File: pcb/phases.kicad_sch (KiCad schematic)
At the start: 50 parts, among them J13 Conn_01x06_Male, SW18 Reset, SW19 +1, SW20 +10, SW21 -10, SW22 -1, SW23 x2, SW24 /2, SW25 Random, U10 74HC595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

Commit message: layout changes
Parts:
- added J14: Conn_01x04_Male, symbol Connector:Conn_01x04_Male
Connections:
- net Button_serial_out: now also J14.4 (Pin_4)
- net Clock: now also J14.2 (Pin_2)
- net Clock_enable: now also J14.3 (Pin_3)
- net Parallel_Load: now also J14.1 (Pin_1)
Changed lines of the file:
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@@
+    (stroke (width 0) (type default) (color 0 0 0 0))
+  )
+  (wire (pts (xy 78.994 83.312) (xy 99.314 83.312))
     (stroke (width 0) (type default) (color 0 0 0 0))
   )
@@
     (stroke (width 0) (type default) (color 0 0 0 0))
   )
+  (wire (pts (xy 78.994 78.232) (xy 99.314 78.232))
+    (stroke (width 0) (type default) (color 0 0 0 0))
+  )
   (wire (pts (xy 238.252 75.438) (xy 238.252 37.338))
     (stroke (width 0) (type default) (color 0 0 0 0))
@@
     (stroke (width 0) (type default) (color 0 0 0 0))
   )
+  (wire (pts (xy 78.994 80.772) (xy 99.314 80.772))
+    (stroke (width 0) (type default) (color 0 0 0 0))
+  )
   (wire (pts (xy 281.432 105.918) (xy 281.432 108.458))
     (stroke (width 0) (type default) (color 0 0 0 0))
@@
   )
   (wire (pts (xy 28.702 67.818) (xy 28.702 69.088))
+    (stroke (width 0) (type default) (color 0 0 0 0))
+  )
+  (wire (pts (xy 78.994 85.852) (xy 99.314 85.852))
     (stroke (width 0) (type default) (color 0 0 0 0))
   )
@@
     (effects (font (size 1.27 1.27)) (justify left bottom))
   )
+  (hierarchical_label "Clock" (shape input) (at 78.994 80.772 180)
+    (effects (font (size 1.27 1.27)) (justify right))
+  )
+  (hierarchical_label "Button_serial_out" (shape output) (at 78.994 85.852 180)
+    (effects (font (size 1.27 1.27)) (justify right))
+  )
   (hierarchical_label "Storage_Register_Clock" (shape input) (at 172.212 78.486 180)
     (effects (font (size 1.27 1.27)) (justify right))
   )
+  (hierarchical_label "Clock_enable" (shape input) (at 78.994 83.312 180)
+    (effects (font (size 1.27 1.27)) (justify right))
+  )
   (hierarchical_label "Serial_Data_Input" (shape input) (at 172.212 73.406 180)
     (effects (font (size 1.27 1.27)) (justify right))
@@
   )
   (hierarchical_label "Storage_Register_Clock" (shape input) (at 184.912 37.338 180)
+    (effects (font (size 1.27 1.27)) (justify right))
+  )
+  (hierarchical_label "Parallel_Load" (shape input) (at 78.994 78.232 180)
     (effects (font (size 1.27 1.27)) (justify right))
   )
@@
     (pin "1")
   )
+  (symbol (lib_id "Connector:Conn_01x04_Male") (at 104.394 80.772 0) (mirror y) (unit 1)
+    (in_bom yes) (on_board yes) (fields_autoplaced)
+    (property "Reference" "J14" (id 0) (at 105.1052 81.2073 0)
+      (effects (font (size 1.27 1.27)) (justify right))
+    )
+    (property "Value" "Conn_01x04_Male" (id 1) (at 105.1052 83.7442 0)
+      (effects (font (size 1.27 1.27)) (justify right))
+    )
+    (property "Footprint" "" (id 2) (at 104.394 80.772 0)
+      (effects (font (size 1.27 1.27)) hide)
+    )
+    (property "Datasheet" "~" (id 3) (at 104.394 80.772 0)
+      (effects (font (size 1.27 1.27)) hide)
+    )
+    (pin "1")
+    (pin "2")
+    (pin "3")
+    (pin "4")
+  )
   (symbol (lib_id "Device:C") (at 28.702 64.008 0) (unit 1)

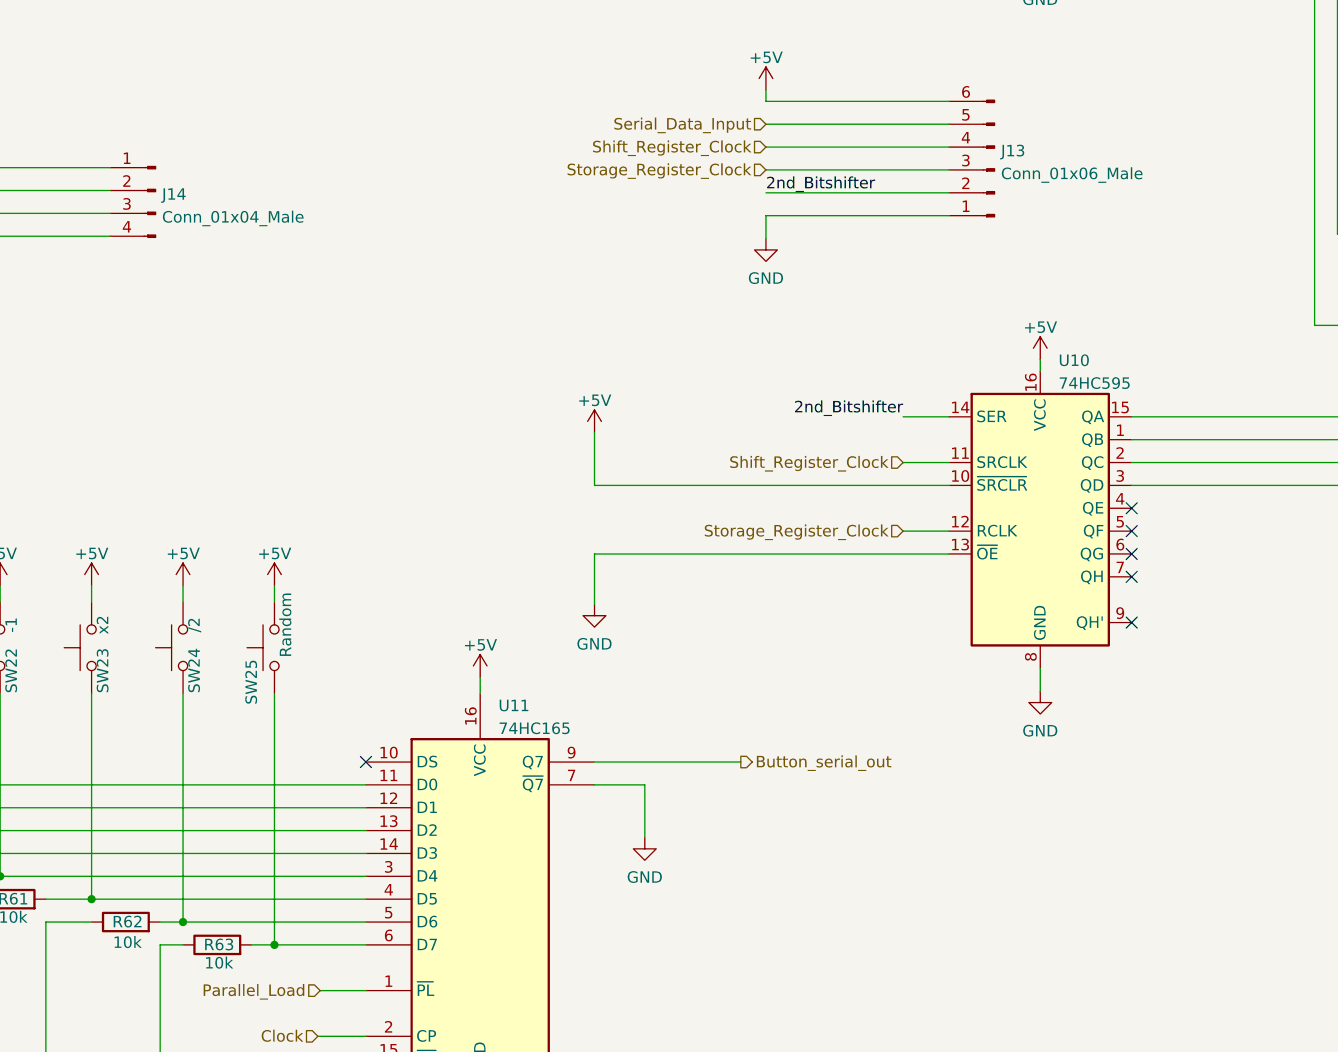
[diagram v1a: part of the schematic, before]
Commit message: moved crystal
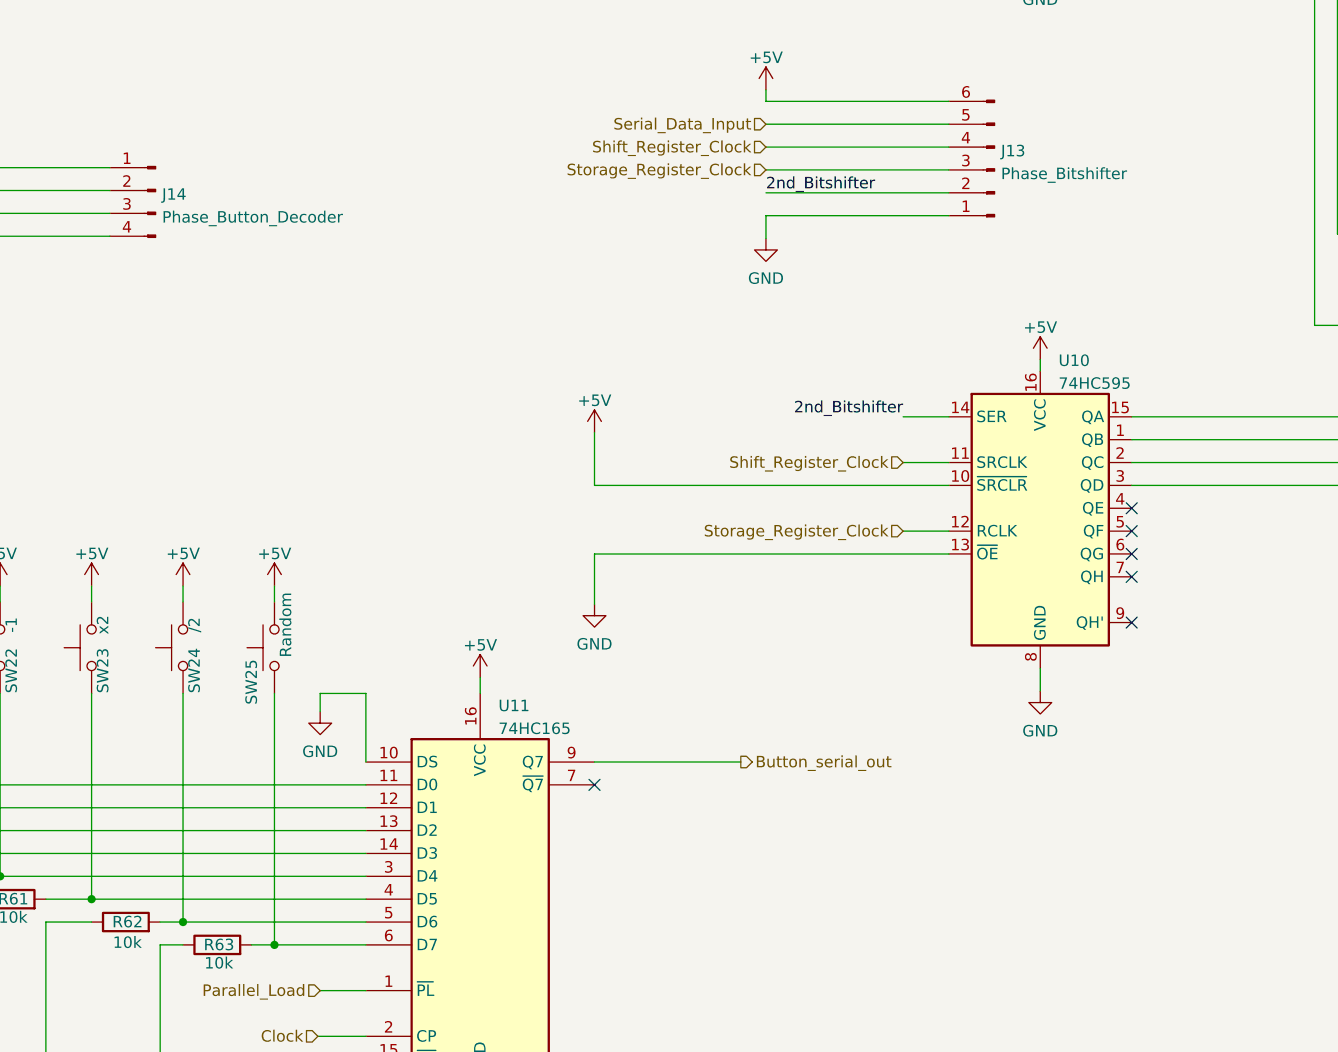
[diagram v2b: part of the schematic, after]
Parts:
- J13: value Conn_01x06_Male -> Phase_Bitshifter
- J14: value Conn_01x04_Male -> Phase_Button_Decoder; footprint (none) -> Connector_PinHeader_2.54mm:PinHeader_1x04_P2.54mm_Vertical
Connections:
- net GND: now also U11.10 (DS); no longer U11.7 (~{Q7})
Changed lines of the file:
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@@
   (no_connect (at 212.852 123.698))
   (no_connect (at 212.852 128.778))
-  (no_connect (at 127.762 144.272))
+  (no_connect (at 153.162 146.812))
   (wire (pts (xy 115.062 164.592) (xy 117.602 164.592))
     (stroke (width 0) (type default) (color 0 0 0 0))
@@
     (stroke (width 0) (type default) (color 0 0 0 0))
   )
+  (wire (pts (xy 122.682 136.652) (xy 122.682 138.684))
+    (stroke (width 0) (type default) (color 0 0 0 0))
+  )
   (wire (pts (xy 46.482 136.652) (xy 46.482 146.812))
     (stroke (width 0) (type default) (color 0 0 0 0))
@@
     (stroke (width 0) (type default) (color 0 0 0 0))
   )
+  (wire (pts (xy 127.762 136.652) (xy 127.762 144.272))
+    (stroke (width 0) (type default) (color 0 0 0 0))
+  )
   (wire (pts (xy 233.172 95.758) (xy 250.952 95.758))
     (stroke (width 0) (type default) (color 0 0 0 0))
@@
     (stroke (width 0) (type default) (color 0 0 0 0))
   )
-  (wire (pts (xy 158.75 146.812) (xy 158.75 152.654))
-    (stroke (width 0) (type default) (color 0 0 0 0))
-  )
   (wire (pts (xy 212.852 47.498) (xy 217.932 47.498))
     (stroke (width 0) (type default) (color 0 0 0 0))
@@
     (stroke (width 0) (type default) (color 0 0 0 0))
   )
+  (wire (pts (xy 122.682 136.652) (xy 127.762 136.652))
+    (stroke (width 0) (type default) (color 0 0 0 0))
+  )
   (wire (pts (xy 212.852 113.538) (xy 245.872 113.538))
     (stroke (width 0) (type default) (color 0 0 0 0))
@@
   )
   (wire (pts (xy 281.432 65.278) (xy 281.432 67.818))
-    (stroke (width 0) (type default) (color 0 0 0 0))
-  )
-  (wire (pts (xy 153.162 146.812) (xy 158.75 146.812))
     (stroke (width 0) (type default) (color 0 0 0 0))
   )
@@
     (pin "1")
   )
+  (symbol (lib_id "power:GND") (at 122.682 138.684 0) (unit 1)
+    (in_bom yes) (on_board yes) (fields_autoplaced)
+    (property "Reference" "#PWR0167" (id 0) (at 122.682 145.034 0)
+      (effects (font (size 1.27 1.27)) hide)
+    )
+    (property "Value" "GND" (id 1) (at 122.682 143.1274 0))
+    (property "Footprint" "" (id 2) (at 122.682 138.684 0)
+      (effects (font (size 1.27 1.27)) hide)
+    )
+    (property "Datasheet" "" (id 3) (at 122.682 138.684 0)
+      (effects (font (size 1.27 1.27)) hide)
+    )
+    (pin "1")
+  )
   (symbol (lib_id "Device:R") (at 270.002 85.598 90) (unit 1)
     (in_bom yes) (on_board yes) (fields_autoplaced)
@@
       (effects (font (size 1.27 1.27)) (justify right))
     )
-    (property "Value" "Conn_01x06_Male" (id 1) (at 198.3232 78.9182 0)
+    (property "Value" "Phase_Bitshifter" (id 1) (at 198.3232 78.9182 0)
       (effects (font (size 1.27 1.27)) (justify right))
     )
@@
     (pin "2")
   )
-  (symbol (lib_id "power:GND") (at 158.75 152.654 0) (unit 1)
-    (in_bom yes) (on_board yes) (fields_autoplaced)
-    (property "Reference" "#PWR081" (id 0) (at 158.75 159.004 0)
-      (effects (font (size 1.27 1.27)) hide)
-    )
-    (property "Value" "GND" (id 1) (at 158.75 157.0974 0))
-    (property "Footprint" "" (id 2) (at 158.75 152.654 0)
-      (effects (font (size 1.27 1.27)) hide)
-    )
-    (property "Datasheet" "" (id 3) (at 158.75 152.654 0)
-      (effects (font (size 1.27 1.27)) hide)
-    )
-    (pin "1")
-  )
   (symbol (lib_id "power:GND") (at 281.432 37.338 0) (unit 1)
     (in_bom yes) (on_board yes) (fields_autoplaced)
@@
       (effects (font (size 1.27 1.27)) (justify right))
     )
-    (property "Value" "Conn_01x04_Male" (id 1) (at 105.1052 83.7442 0)
+    (property "Value" "Phase_Button_Decoder" (id 1) (at 105.1052 83.7442 0)
       (effects (font (size 1.27 1.27)) (justify right))
     )
-    (property "Footprint" "" (id 2) (at 104.394 80.772 0)
-      (effects (font (size 1.27 1.27)) hide)
-    )
+    (property "Footprint" "Connector_PinHeader_2.54mm:PinHeader_1x04_P2.54mm_Vertical" (id 2) (at 104.394 80.772 0)
+      (effects (font (size 1.27 1.27)) hide)
+    )

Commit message: new layout with usb
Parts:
- R44, R45, R46, R47, R48, R49, R50, R51, R52, R53, R54, R55, R56, R57, R58, R59, R60, R61, R62, R63: footprint Resistor_THT:R_Axial_DIN0207_L6.3mm_D2.5mm_P7.62mm_Horizontal -> Resistor_THT:R_Axial_DIN0207_L6.3mm_D2.5mm_P10.16mm_Horizontal
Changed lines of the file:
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@@
     (property "Reference" "R54" (id 0) (at 270.002 121.5222 90))
     (property "Value" "90R" (id 1) (at 270.002 124.0591 90))
-    (property "Footprint" "Resistor_THT:R_Axial_DIN0207_L6.3mm_D2.5mm_P7.62mm_Horizontal" (id 2) (at 270.002 128.016 90)
+    (property "Footprint" "Resistor_THT:R_Axial_DIN0207_L6.3mm_D2.5mm_P10.16mm_Horizontal" (id 2) (at 270.002 128.016 90)
       (effects (font (size 1.27 1.27)) hide)
     )
@@
     (property "Reference" "R44" (id 0) (at 270.002 19.9222 90))
     (property "Value" "90R" (id 1) (at 270.002 22.4591 90))
-    (property "Footprint" "Resistor_THT:R_Axial_DIN0207_L6.3mm_D2.5mm_P7.62mm_Horizontal" (id 2) (at 270.002 26.416 90)
+    (property "Footprint" "Resistor_THT:R_Axial_DIN0207_L6.3mm_D2.5mm_P10.16mm_Horizontal" (id 2) (at 270.002 26.416 90)
       (effects (font (size 1.27 1.27)) hide)
     )
@@
       (effects (font (size 1.27 1.27)) (justify left))
     )
-    (property "Footprint" "Resistor_THT:R_Axial_DIN0207_L6.3mm_D2.5mm_P7.62mm_Horizontal" (id 2) (at 63.246 156.21 90)
+    (property "Footprint" "Resistor_THT:R_Axial_DIN0207_L6.3mm_D2.5mm_P10.16mm_Horizontal" (id 2) (at 63.246 156.21 90)
       (effects (font (size 1.27 1.27)) hide)
     )
@@
       (effects (font (size 1.27 1.27)) (justify left))
     )
-    (property "Footprint" "Resistor_THT:R_Axial_DIN0207_L6.3mm_D2.5mm_P7.62mm_Horizontal" (id 2) (at 101.092 163.83 90)
+    (property "Footprint" "Resistor_THT:R_Axial_DIN0207_L6.3mm_D2.5mm_P10.16mm_Horizontal" (id 2) (at 101.092 163.83 90)
       (effects (font (size 1.27 1.27)) hide)
     )
@@
     (property "Reference" "R50" (id 0) (at 270.002 80.8822 90))
     (property "Value" "90R" (id 1) (at 270.002 83.4191 90))
-    (property "Footprint" "Resistor_THT:R_Axial_DIN0207_L6.3mm_D2.5mm_P7.62mm_Horizontal" (id 2) (at 270.002 87.376 90)
+    (property "Footprint" "Resistor_THT:R_Axial_DIN0207_L6.3mm_D2.5mm_P10.16mm_Horizontal" (id 2) (at 270.002 87.376 90)
       (effects (font (size 1.27 1.27)) hide)
     )
@@
       (effects (font (size 1.27 1.27)) (justify left))
     )
-    (property "Footprint" "Resistor_THT:R_Axial_DIN0207_L6.3mm_D2.5mm_P7.62mm_Horizontal" (id 2) (at 37.592 151.13 90)
+    (property "Footprint" "Resistor_THT:R_Axial_DIN0207_L6.3mm_D2.5mm_P10.16mm_Horizontal" (id 2) (at 37.592 151.13 90)
       (effects (font (size 1.27 1.27)) hide)
     )
@@
     (property "Reference" "R51" (id 0) (at 270.002 91.0422 90))
     (property "Value" "90R" (id 1) (at 270.002 93.5791 90))
-    (property "Footprint" "Resistor_THT:R_Axial_DIN0207_L6.3mm_D2.5mm_P7.62mm_Horizontal" (id 2) (at 270.002 97.536 90)
+    (property "Footprint" "Resistor_THT:R_Axial_DIN0207_L6.3mm_D2.5mm_P10.16mm_Horizontal" (id 2) (at 270.002 97.536 90)
       (effects (font (size 1.27 1.27)) hide)
     )
@@
       (effects (font (size 1.27 1.27)) (justify left))
     )
-    (property "Footprint" "Resistor_THT:R_Axial_DIN0207_L6.3mm_D2.5mm_P7.62mm_Horizontal" (id 2) (at 111.252 166.37 90)
+    (property "Footprint" "Resistor_THT:R_Axial_DIN0207_L6.3mm_D2.5mm_P10.16mm_Horizontal" (id 2) (at 111.252 166.37 90)
       (effects (font (size 1.27 1.27)) hide)
     )
@@
       (effects (font (size 1.27 1.27)) (justify left))
     )
-    (property "Footprint" "Resistor_THT:R_Axial_DIN0207_L6.3mm_D2.5mm_P7.62mm_Horizontal" (id 2) (at 75.692 158.75 90)
+    (property "Footprint" "Resistor_THT:R_Axial_DIN0207_L6.3mm_D2.5mm_P10.16mm_Horizontal" (id 2) (at 75.692 158.75 90)
       (effects (font (size 1.27 1.27)) hide)
     )
@@
     (property "Reference" "R52" (id 0) (at 270.002 101.2022 90))
     (property "Value" "90R" (id 1) (at 270.002 103.7391 90))
-    (property "Footprint" "Resistor_THT:R_Axial_DIN0207_L6.3mm_D2.5mm_P7.62mm_Horizontal" (id 2) (at 270.002 107.696 90)
+    (property "Footprint" "Resistor_THT:R_Axial_DIN0207_L6.3mm_D2.5mm_P10.16mm_Horizontal" (id 2) (at 270.002 107.696 90)
       (effects (font (size 1.27 1.27)) hide)
     )
@@
     (property "Reference" "R46" (id 0) (at 270.002 40.2422 90))
     (property "Value" "90R" (id 1) (at 270.002 42.7791 90))
-    (property "Footprint" "Resistor_THT:R_Axial_DIN0207_L6.3mm_D2.5mm_P7.62mm_Horizontal" (id 2) (at 270.002 46.736 90)
+    (property "Footprint" "Resistor_THT:R_Axial_DIN0207_L6.3mm_D2.5mm_P10.16mm_Horizontal" (id 2) (at 270.002 46.736 90)
       (effects (font (size 1.27 1.27)) hide)
     )
@@
     (property "Reference" "R49" (id 0) (at 270.002 70.7222 90))
     (property "Value" "90R" (id 1) (at 270.002 73.2591 90))
-    (property "Footprint" "Resistor_THT:R_Axial_DIN0207_L6.3mm_D2.5mm_P7.62mm_Horizontal" (id 2) (at 270.002 77.216 90)
+    (property "Footprint" "Resistor_THT:R_Axial_DIN0207_L6.3mm_D2.5mm_P10.16mm_Horizontal" (id 2) (at 270.002 77.216 90)
       (effects (font (size 1.27 1.27)) hide)
     )
@@
     (property "Reference" "R48" (id 0) (at 270.002 60.5622 90))
     (property "Value" "90R" (id 1) (at 270.002 63.0991 90))
-    (property "Footprint" "Resistor_THT:R_Axial_DIN0207_L6.3mm_D2.5mm_P7.62mm_Horizontal" (id 2) (at 270.002 67.056 90)
+    (property "Footprint" "Resistor_THT:R_Axial_DIN0207_L6.3mm_D2.5mm_P10.16mm_Horizontal" (id 2) (at 270.002 67.056 90)
       (effects (font (size 1.27 1.27)) hide)
     )
@@
       (effects (font (size 1.27 1.27)) (justify left))
     )
-    (property "Footprint" "Resistor_THT:R_Axial_DIN0207_L6.3mm_D2.5mm_P7.62mm_Horizontal" (id 2) (at 50.292 153.67 90)
+    (property "Footprint" "Resistor_THT:R_Axial_DIN0207_L6.3mm_D2.5mm_P10.16mm_Horizontal" (id 2) (at 50.292 153.67 90)
       (effects (font (size 1.27 1.27)) hide)
     )
@@
       (effects (font (size 1.27 1.27)) (justify left))
     )
-    (property "Footprint" "Resistor_THT:R_Axial_DIN0207_L6.3mm_D2.5mm_P7.62mm_Horizontal" (id 2) (at 88.392 161.29 90)
+    (property "Footprint" "Resistor_THT:R_Axial_DIN0207_L6.3mm_D2.5mm_P10.16mm_Horizontal" (id 2) (at 88.392 161.29 90)
       (effects (font (size 1.27 1.27)) hide)
     )
@@
     (property "Reference" "R53" (id 0) (at 270.002 111.3622 90))
     (property "Value" "90R" (id 1) (at 270.002 113.8991 90))
-    (property "Footprint" "Resistor_THT:R_Axial_DIN0207_L6.3mm_D2.5mm_P7.62mm_Horizontal" (id 2) (at 270.002 117.856 90)
+    (property "Footprint" "Resistor_THT:R_Axial_DIN0207_L6.3mm_D2.5mm_P10.16mm_Horizontal" (id 2) (at 270.002 117.856 90)
       (effects (font (size 1.27 1.27)) hide)
     )
@@
       (effects (font (size 1.27 1.27)) (justify left))
     )
-    (property "Footprint" "Resistor_THT:R_Axial_DIN0207_L6.3mm_D2.5mm_P7.62mm_Horizontal" (id 2) (at 24.892 148.59 90)
+    (property "Footprint" "Resistor_THT:R_Axial_DIN0207_L6.3mm_D2.5mm_P10.16mm_Horizontal" (id 2) (at 24.892 148.59 90)
       (effects (font (size 1.27 1.27)) hide)
     )
@@
     (property "Reference" "R45" (id 0) (at 270.002 30.0822 90))
     (property "Value" "90R" (id 1) (at 270.002 32.6191 90))
-    (property "Footprint" "Resistor_THT:R_Axial_DIN0207_L6.3mm_D2.5mm_P7.62mm_Horizontal" (id 2) (at 270.002 36.576 90)
+    (property "Footprint" "Resistor_THT:R_Axial_DIN0207_L6.3mm_D2.5mm_P10.16mm_Horizontal" (id 2) (at 270.002 36.576 90)
       (effects (font (size 1.27 1.27)) hide)
     )
@@
     (property "Reference" "R47" (id 0) (at 270.002 50.4022 90))
     (property "Value" "90R" (id 1) (at 270.002 52.9391 90))
-    (property "Footprint" "Resistor_THT:R_Axial_DIN0207_L6.3mm_D2.5mm_P7.62mm_Horizontal" (id 2) (at 270.002 56.896 90)
+    (property "Footprint" "Resistor_THT:R_Axial_DIN0207_L6.3mm_D2.5mm_P10.16mm_Horizontal" (id 2) (at 270.002 56.896 90)
       (effects (font (size 1.27 1.27)) hide)
     )
@@
     (property "Reference" "R55" (id 0) (at 270.002 131.6822 90))
     (property "Value" "90R" (id 1) (at 270.002 134.2191 90))
-    (property "Footprint" "Resistor_THT:R_Axial_DIN0207_L6.3mm_D2.5mm_P7.62mm_Horizontal" (id 2) (at 270.002 138.176 90)
-      (effects (font (size 1.27 1.27)) hide)
-    )
+    (property "Footprint" "Resistor_THT:R_Axial_DIN0207_L6.3mm_D2.5mm_P10.16mm_Horizontal" (id 2) (at 270.002 138.176 90)
+      (effects (font (size 1.27 1.27)) hide)
+    )
